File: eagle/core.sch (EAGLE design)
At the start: 19 parts, among them K1 AQH2223A, SW0 TPTP10R, SW1 TPTP10R

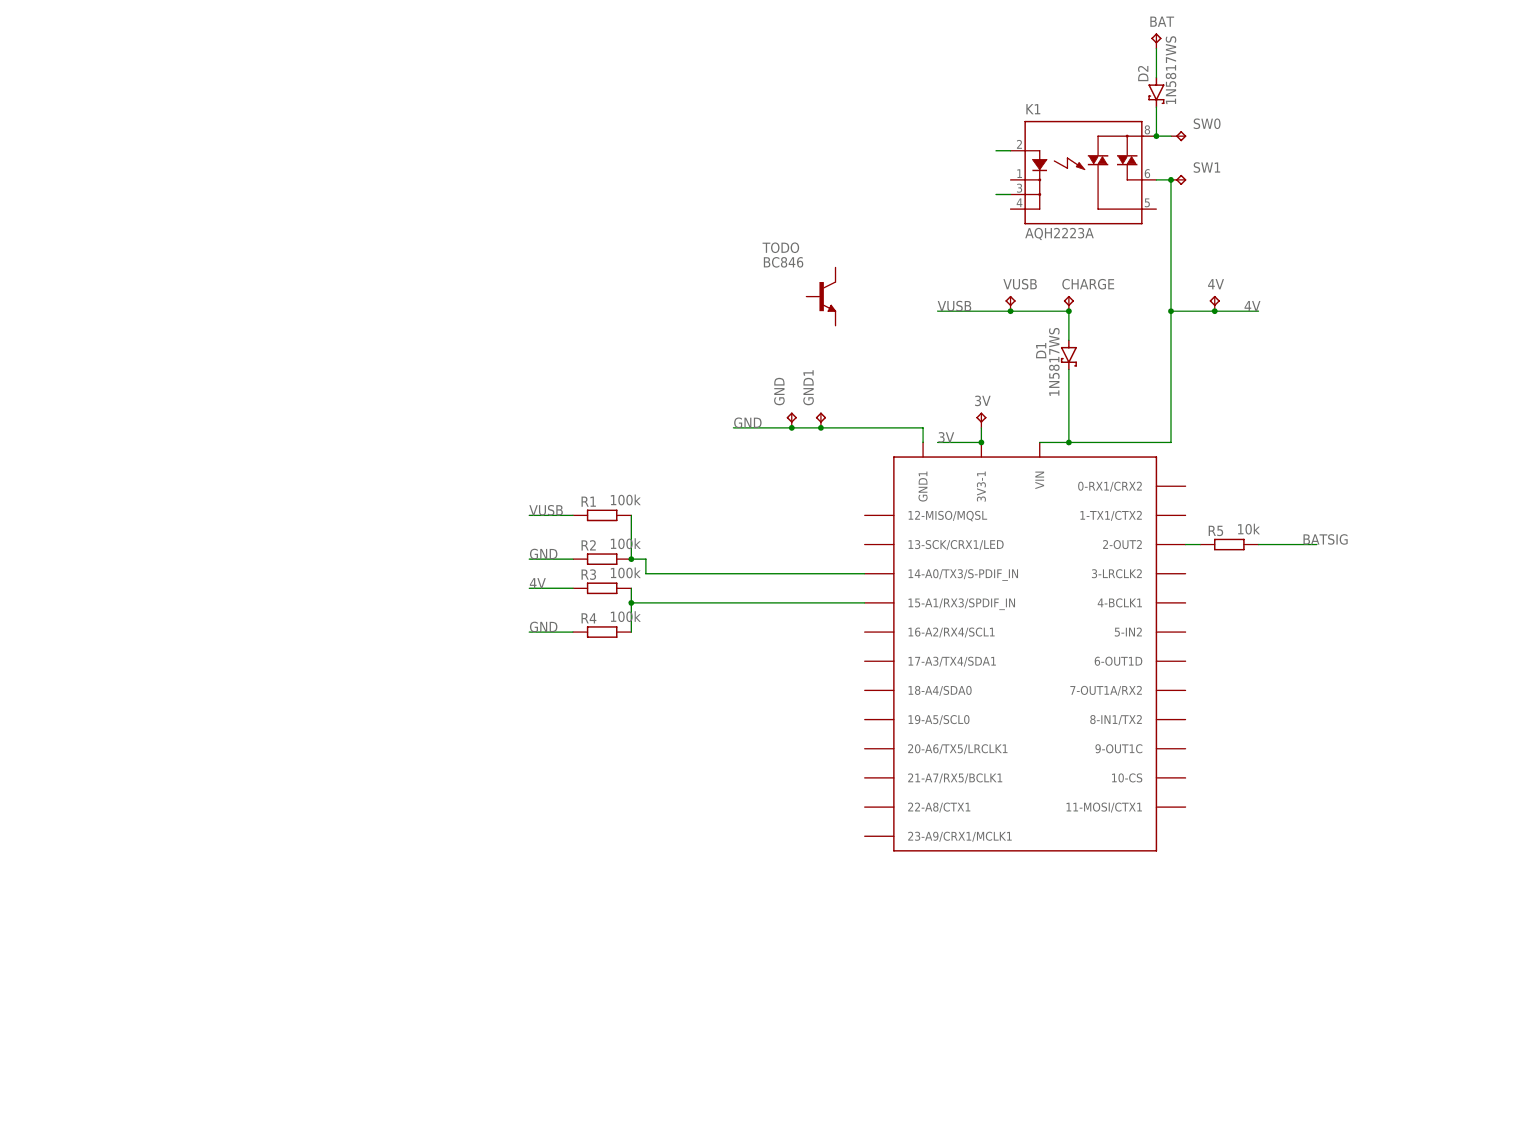
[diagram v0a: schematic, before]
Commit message: add torch and uv schematic
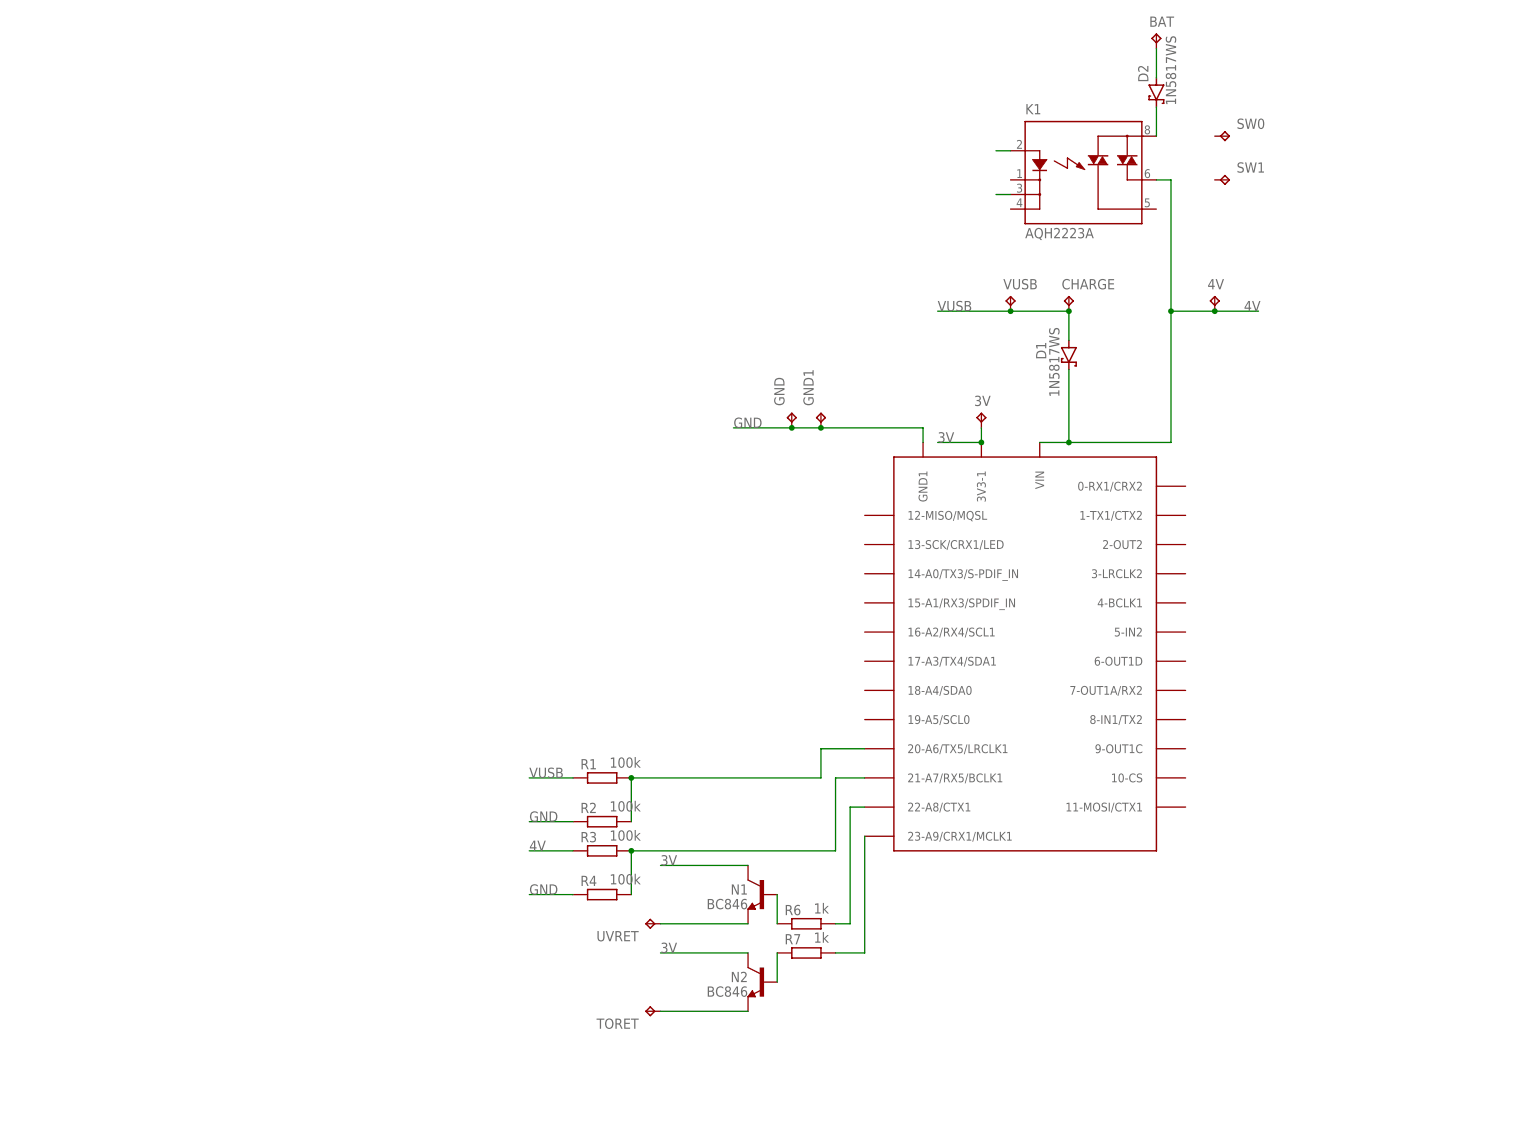
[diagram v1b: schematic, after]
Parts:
- removed R5: 10k, resistor:R-EU_M0805
- removed TODO: BC846, transistor:BC846
- added N1, N2: BC846, transistor:BC846
- added R6, R7: 1k, resistor:R-EU_M0805
- added TORET, UVRET: TPTP10R, testpad:TPTP10R
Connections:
- removed net BATSIG: R5.2
- removed net N$3: R5.1, U$1.2-OUT2
- new net N$10: N1.B, R6.1
- new net N$11: N2.B, R7.1
- new net N$12: N1.E, UVRET.TP
- new net N$13: N2.E, TORET.TP
- new net N$8: R7.2, U$1.23-A9/CRX1/MCLK1
- new net N$9: R6.2, U$1.22-A8/CTX1
- net 3V: now also N1.C, N2.C
- net 4V: no longer SW1.TP
- net N$2: now also U$1.21-A7/RX5/BCLK1; no longer U$1.15-A1/RX3/SPDIF_IN
- net N$5: no longer SW0.TP
- net N$6: now also U$1.20-A6/TX5/LRCLK1; no longer U$1.14-A0/TX3/S-PDIF_IN
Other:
- moved on the sheet: R1, R2, R3, R4, SW0, SW1

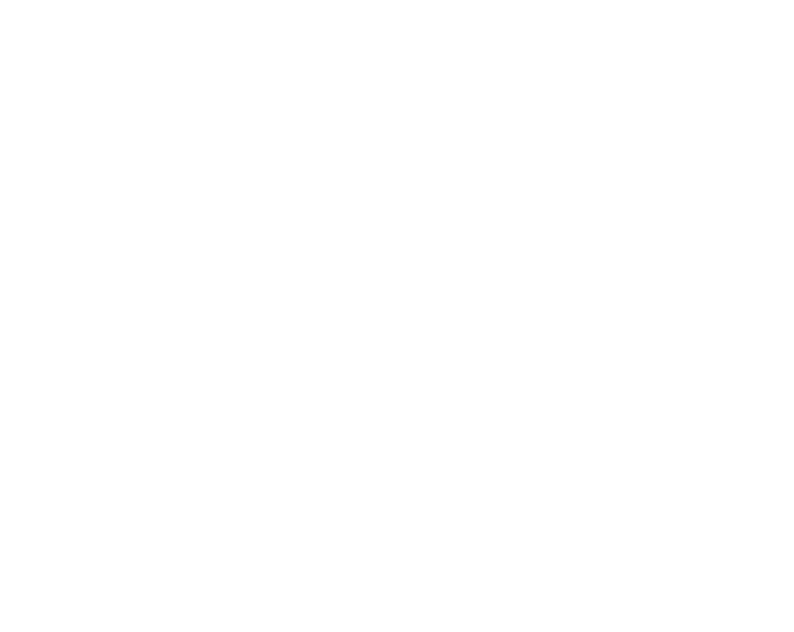
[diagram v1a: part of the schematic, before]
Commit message: Display board redesigned with FFC connector
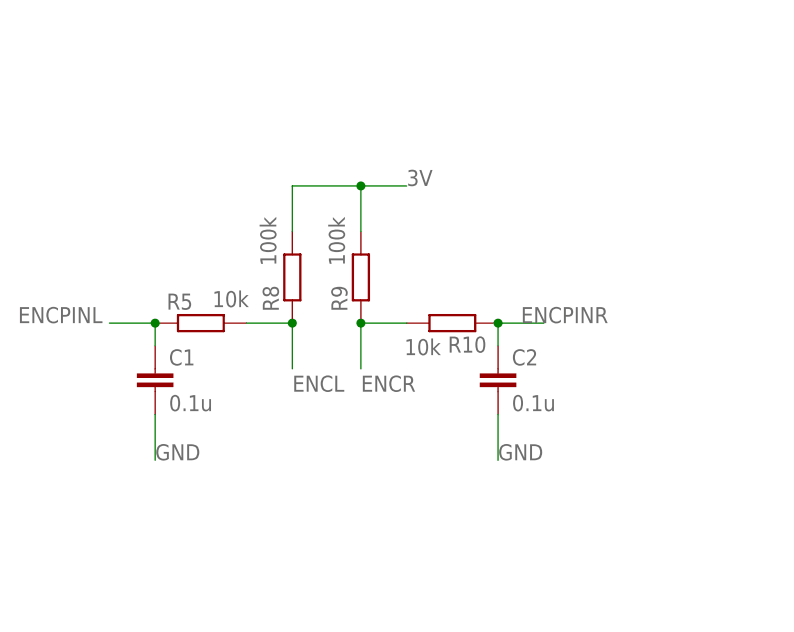
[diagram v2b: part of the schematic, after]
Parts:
- added C1, C2: 0.1u, resistor:C-EUC0805
- added R10, R5: 10k, resistor:R-EU_M0805
- added R8, R9: 100k, resistor:R-EU_M0805
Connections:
- new net ENCL: R5.2, R8.1
- new net ENCPINL: C1.1, R5.1
- new net ENCPINR: C2.1, R10.1
- new net ENCR: R10.2, R9.1
- net 3V: now also R8.2, R9.2
- net GND: now also C1.2, C2.2
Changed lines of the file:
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@@
 <part name="UVRET" library="testpad" library_urn="urn:adsk.eagle:library:385" deviceset="TP" device="TP10R" package3d_urn="urn:adsk.eagle:package:27959/1"/>
 <part name="TORET" library="testpad" library_urn="urn:adsk.eagle:library:385" deviceset="TP" device="TP10R" package3d_urn="urn:adsk.eagle:package:27959/1"/>
+<part name="R5" library="resistor" library_urn="urn:adsk.eagle:library:348" deviceset="R-EU_" device="M0805" package3d_urn="urn:adsk.eagle:package:23556/2" value="10k"/>
+<part name="R8" library="resistor" library_urn="urn:adsk.eagle:library:348" deviceset="R-EU_" device="M0805" package3d_urn="urn:adsk.eagle:package:23556/2" value="100k"/>
+<part name="R9" library="resistor" library_urn="urn:adsk.eagle:library:348" deviceset="R-EU_" device="M0805" package3d_urn="urn:adsk.eagle:package:23556/2" value="100k"/>
+<part name="R10" library="resistor" library_urn="urn:adsk.eagle:library:348" deviceset="R-EU_" device="M0805" package3d_urn="urn:adsk.eagle:package:23556/2" value="10k"/>
+<part name="C1" library="resistor" library_urn="urn:adsk.eagle:library:348" deviceset="C-EU" device="C0805" package3d_urn="urn:adsk.eagle:package:23617/2" value="0.1u"/>
+<part name="C2" library="resistor" library_urn="urn:adsk.eagle:library:348" deviceset="C-EU" device="C0805" package3d_urn="urn:adsk.eagle:package:23617/2" value="0.1u"/>
 </parts>
 <sheets>
@@
 <attribute name="NAME" x="-102.87" y="-19.05" size="1.778" layer="95" rot="R180"/>
 <attribute name="TP_SIGNAL_NAME" x="-100.33" y="-16.51" size="1.778" layer="97" rot="R90"/>
+</instance>
+<instance part="R5" gate="G$1" x="-170.18" y="119.38" smashed="yes">
+<attribute name="NAME" x="-173.99" y="120.8786" size="1.778" layer="95"/>
+<attribute name="VALUE" x="-168.91" y="121.158" size="1.778" layer="96"/>
+</instance>
+<instance part="R8" gate="G$1" x="-160.02" y="124.46" smashed="yes" rot="R90">
+<attribute name="NAME" x="-161.5186" y="120.65" size="1.778" layer="95" rot="R90"/>
+<attribute name="VALUE" x="-161.798" y="125.73" size="1.778" layer="96" rot="R90"/>
+</instance>
+<instance part="R9" gate="G$1" x="-152.4" y="124.46" smashed="yes" rot="R90">
+<attribute name="NAME" x="-153.8986" y="120.65" size="1.778" layer="95" rot="R90"/>
+<attribute name="VALUE" x="-154.178" y="125.73" size="1.778" layer="96" rot="R90"/>
+</instance>
+<instance part="R10" gate="G$1" x="-142.24" y="119.38" smashed="yes" rot="R180">
+<attribute name="NAME" x="-138.43" y="117.8814" size="1.778" layer="95" rot="R180"/>
+<attribute name="VALUE" x="-143.51" y="117.602" size="1.778" layer="96" rot="R180"/>
+</instance>
+<instance part="C1" gate="G$1" x="-175.26" y="114.3" smashed="yes">
+<attribute name="NAME" x="-173.736" y="114.681" size="1.778" layer="95"/>
+<attribute name="VALUE" x="-173.736" y="109.601" size="1.778" layer="96"/>
+</instance>
+<instance part="C2" gate="G$1" x="-137.16" y="114.3" smashed="yes">
+<attribute name="NAME" x="-135.636" y="114.681" size="1.778" layer="95"/>
+<attribute name="VALUE" x="-135.636" y="109.601" size="1.778" layer="96"/>
 </instance>
 </instances>
@@
 <label x="-121.92" y="2.54" size="1.778" layer="95"/>
 </segment>
+<segment>
+<pinref part="C1" gate="G$1" pin="2"/>
+<wire x1="-175.26" y1="109.22" x2="-175.26" y2="104.14" width="0.1524" layer="91"/>
+<label x="-175.26" y="104.14" size="1.778" layer="95"/>
+</segment>
+<segment>
+<pinref part="C2" gate="G$1" pin="2"/>
+<wire x1="-137.16" y1="109.22" x2="-137.16" y2="104.14" width="0.1524" layer="91"/>
+<label x="-137.16" y="104.14" size="1.778" layer="95"/>
+</segment>
 </net>
 <net name="N$6" class="0">
@@
 <label x="-99.06" y="-7.62" size="1.778" layer="95"/>
 </segment>
+<segment>
+<pinref part="R8" gate="G$1" pin="2"/>
+<wire x1="-160.02" y1="129.54" x2="-160.02" y2="134.62" width="0.1524" layer="91"/>
+<wire x1="-160.02" y1="134.62" x2="-152.4" y2="134.62" width="0.1524" layer="91"/>
+<pinref part="R9" gate="G$1" pin="2"/>
+<wire x1="-152.4" y1="134.62" x2="-147.32" y2="134.62" width="0.1524" layer="91"/>
+<wire x1="-152.4" y1="129.54" x2="-152.4" y2="134.62" width="0.1524" layer="91"/>
+<junction x="-152.4" y="134.62"/>
+<label x="-147.32" y="134.62" size="1.778" layer="95"/>
+</segment>
 </net>
 <net name="N$5" class="1">
@@
 </segment>
 </net>
+<net name="ENCL" class="0">
+<segment>
+<pinref part="R8" gate="G$1" pin="1"/>
+<wire x1="-160.02" y1="119.38" x2="-160.02" y2="114.3" width="0.1524" layer="91"/>
+<label x="-160.02" y="111.76" size="1.778" layer="95"/>
+<pinref part="R5" gate="G$1" pin="2"/>
+<wire x1="-165.1" y1="119.38" x2="-160.02" y2="119.38" width="0.1524" layer="91"/>
+<junction x="-160.02" y="119.38"/>
+</segment>
+</net>
+<net name="ENCR" class="0">
+<segment>
+<pinref part="R9" gate="G$1" pin="1"/>
+<wire x1="-152.4" y1="119.38" x2="-152.4" y2="114.3" width="0.1524" layer="91"/>
+<label x="-152.4" y="111.76" size="1.778" layer="95"/>
+<pinref part="R10" gate="G$1" pin="2"/>
+<wire x1="-147.32" y1="119.38" x2="-152.4" y2="119.38" width="0.1524" layer="91"/>
+<junction x="-152.4" y="119.38"/>
+</segment>
+</net>
+<net name="ENCPINL" class="0">
+<segment>
+<pinref part="R5" gate="G$1" pin="1"/>
+<wire x1="-175.26" y1="119.38" x2="-180.34" y2="119.38" width="0.1524" layer="91"/>
+<label x="-190.5" y="119.38" size="1.778" layer="95"/>
+<pinref part="C1" gate="G$1" pin="1"/>
+<wire x1="-175.26" y1="116.84" x2="-175.26" y2="119.38" width="0.1524" layer="91"/>
+<junction x="-175.26" y="119.38"/>
+</segment>
+</net>
+<net name="ENCPINR" class="0">
+<segment>
+<pinref part="R10" gate="G$1" pin="1"/>
+<wire x1="-137.16" y1="119.38" x2="-132.08" y2="119.38" width="0.1524" layer="91"/>
+<label x="-134.62" y="119.38" size="1.778" layer="95"/>
+<pinref part="C2" gate="G$1" pin="1"/>
+<wire x1="-137.16" y1="116.84" x2="-137.16" y2="119.38" width="0.1524" layer="91"/>
+<junction x="-137.16" y="119.38"/>
+</segment>
+</net>

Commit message: ffc breakout and core changes
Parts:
- removed 3V, 4V, BAT, CHARGE, GND, GND1, SW0, SW1, TORET, UVRET, VUSB: TPTP10R, testpad:TPTP10R
- removed D1, D2: 1N5817WS, general:1N5817WS
- removed K1: AQH2223A, relay:AQH2223A
- removed N1, N2: BC846, transistor:BC846
- added C3, C4: 10u, resistor:C-EUC0805
- added ENCL, ENCR, MBTN, SBTN, TODO, TODO1: TPTP10R, testpad:TPTP10R
- added R11, R12: 10k, resistor:R-EU_M0805
- added U$2: TEENSYSMALL, general:TEENSYSMALL
- added U$3: 16PINFFC, general:16PINFFC
- R1, R2, R3, R4: value 100k -> 20M
- R6, R7: value 1k -> 10k
- R8, R9: value 100k -> 10k
- U$1: value TEENSY40EDGES -> TEENSY4; device general:TEENSY40EDGES -> general:TEENSYSMALL
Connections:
- removed net N$1: K1.A
- removed net N$10: N1.B, R6.1
- removed net N$11: N2.B, R7.1
- removed net N$12: N1.E, UVRET.TP
- removed net N$13: N2.E, TORET.TP
- removed net N$2: R3.2, R4.2, U$1.21-A7/RX5/BCLK1
- removed net N$4: BAT.TP, D2.A
- removed net N$5: D2.C, K1.DS1
- removed net N$6: R1.2, R2.2, U$1.20-A6/TX5/LRCLK1
- removed net N$7: K1.K1
- removed net N$8: R7.2, U$1.23-A9/CRX1/MCLK1
- removed net N$9: R6.2, U$1.22-A8/CTX1
- removed net VUSB: CHARGE.TP, D1.A, R1.1, VUSB.TP
- new net ANTT1: R1.1, R2.2, U$1.14
- new net ANTT2: R3.1, R4.2, U$1.15
- new net BCLK: U$3.12
- new net DC: U$3.5
- new net DOUT: U$3.11
- new net LRCL: U$3.10
- new net MBTN: MBTN.TP, R11.1, R12.2
- new net MBTNPIN: C4.1, R12.1, TODO.TP
- new net MOSI: U$3.3
- new net PWM1: U$1.5, U$3.16
- new net PWM2: U$1.4, U$3.15
- new net PWM3: U$1.3, U$3.14
- new net PWM4: U$1.2, U$3.13
- new net SBTN: R6.1, R7.2, SBTN.TP
- new net SBTNPIN: C3.1, R7.1, TODO1.TP
- new net SCK: U$3.4
- new net SSCL: U$3.2
- new net SSDA: U$3.1
- new net T4RX: U$1.0, U$2.1
- new net T4TX: U$1.1, U$2.0
- new net TFTCS: U$3.7
- new net TFTRST: U$3.6
- net 3V: now also R1.2, R11.2, R3.2, R6.2, U$1.3V, U$2.3V; no longer 3V.TP, N1.C, N2.C, U$1.3V3-1
- net 4V: no longer 4V.TP, D1.C, K1.DS3, R3.1
- net ENCL: now also ENCL.TP
- net ENCPINL: now also U$2.3
- net ENCPINR: now also U$2.4
- net ENCR: now also ENCR.TP
- net GND: now also C3.2, C4.2, U$1.GND, U$2.GND, U$3.BASE; no longer GND.TP, GND1.TP, U$1.GND1
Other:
- note added: "Teensy 3.2"
- note added: "Teensy 4"
- moved on the sheet: R1, R2, R3, R4, R6, R7

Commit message: mini probe
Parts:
- removed U$3: 16PINFFC, general:16PINFFC
- added 3V, BCLK, DOUT, GND, L1-, L2-, L3-, L4-, LRCL, SSCL, SSDA: TPTP16R, testpad:TPTP16R
- added IC5: APX803, adafruit:AXP083-SAG
- added LED1: (no value), led:LED3MM
- added R13: 10K, microbuilder:RESISTOR_0603_NOOUT
- added R14: 22, microbuilder:RESISTOR_0603_NOOUT
- added R15, R16, R17, R18: (no value), resistor:R-EU_R0805
- added T1, T2, T3, T4: BC846, transistor:BC846
- added U$4: TFT, general:TFT
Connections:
- new net !TFTRST: IC5./RESET, R13.1
- new net L1-: L1-.TP, T1.C
- new net L2-: L2-.TP, T2.C
- new net L3-: L3-.TP, T3.C
- new net L4-: L4-.TP, LED1.C, T4.C
- new net N$1: R14.2, U$4.LEDK
- new net N$2: R15.2, T1.B
- new net N$3: R16.2, T2.B
- new net N$4: R17.2, T3.B
- new net N$5: R18.2, T4.B
- net 3V: now also 3V.TP, IC5.VCC, LED1.A, R13.2, U$4.LEDA, U$4.VDD
- net BCLK: now also BCLK.TP; no longer U$3.12
- net DC: now also U$1.9, U$4.RS/DC; no longer U$3.5
- net DOUT: now also DOUT.TP; no longer U$3.11
- net GND: now also GND.TP, IC5.GND, R14.1, T1.E, T2.E, T3.E, T4.E, U$4.GND; no longer U$3.BASE
- net LRCL: now also LRCL.TP; no longer U$3.10
- net MOSI: now also U$1.11, U$4.DATA; no longer U$3.3
- net PWM1: now also R15.1; no longer U$3.16
- net PWM2: now also R16.1; no longer U$3.15
- net PWM3: now also R17.1; no longer U$3.14
- net PWM4: now also R18.1; no longer U$3.13
- net SCK: now also U$1.13, U$4.CLOCK; no longer U$3.4
- net SSCL: now also SSCL.TP; no longer U$3.2
- net SSDA: now also SSDA.TP; no longer U$3.1
- net TFTCS: now also U$1.10, U$4.CS; no longer U$3.7
- net TFTRST: now also U$1.7, U$4.RESET; no longer U$3.6
